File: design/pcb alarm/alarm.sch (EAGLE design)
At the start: 5 parts, among them IC1 7805T

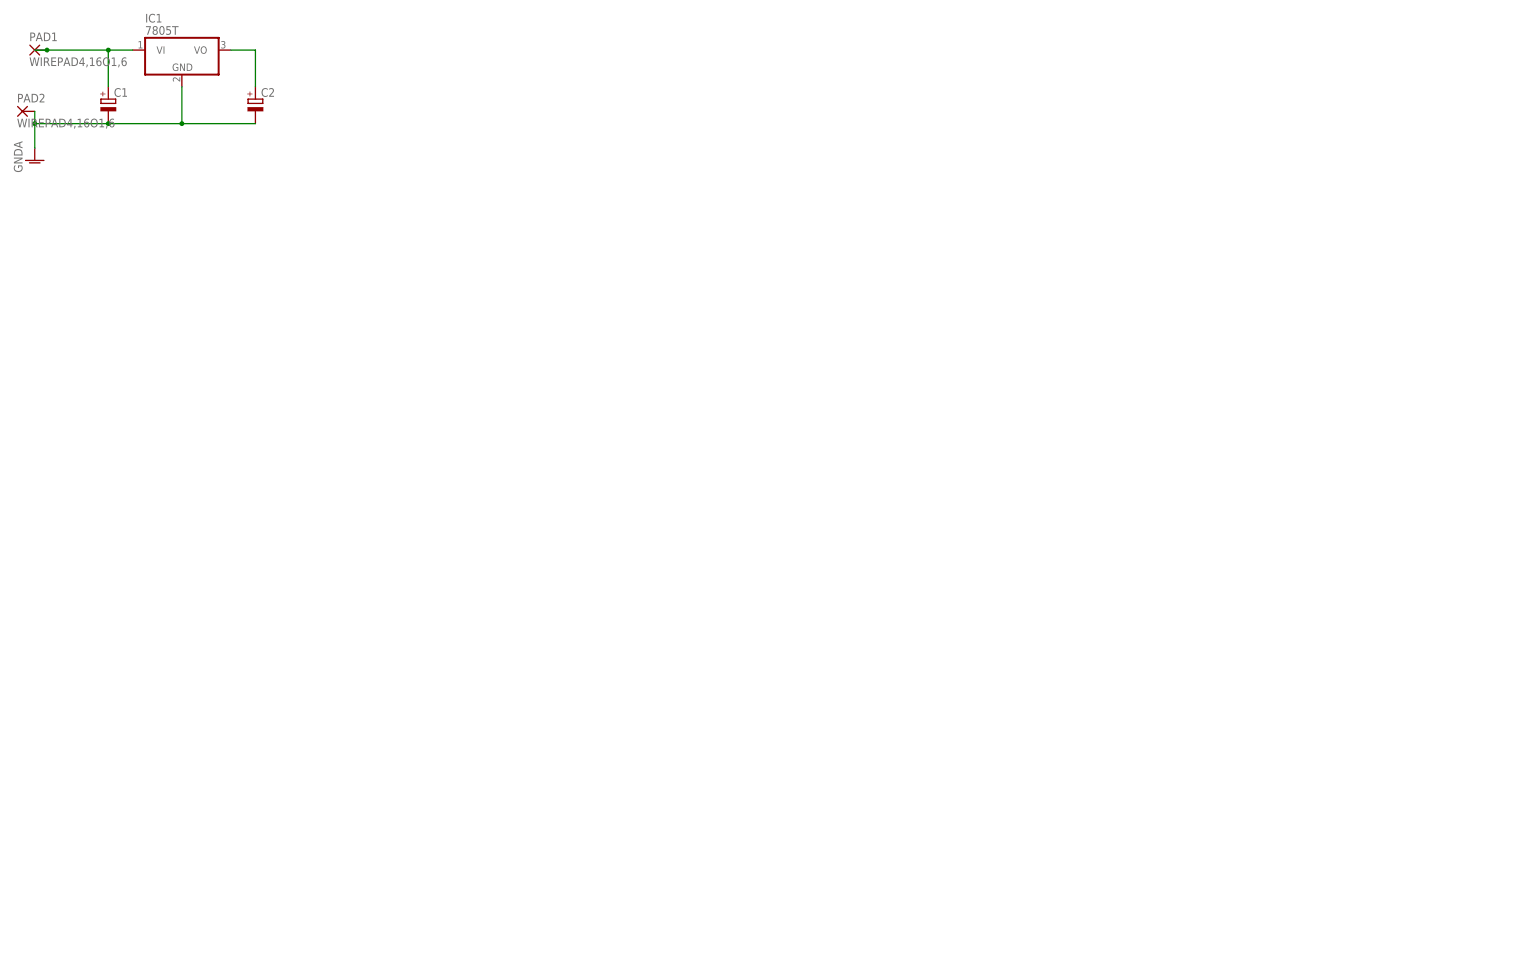
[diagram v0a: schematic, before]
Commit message: 8
pembuatan desain alarm esw untuk ews banjir
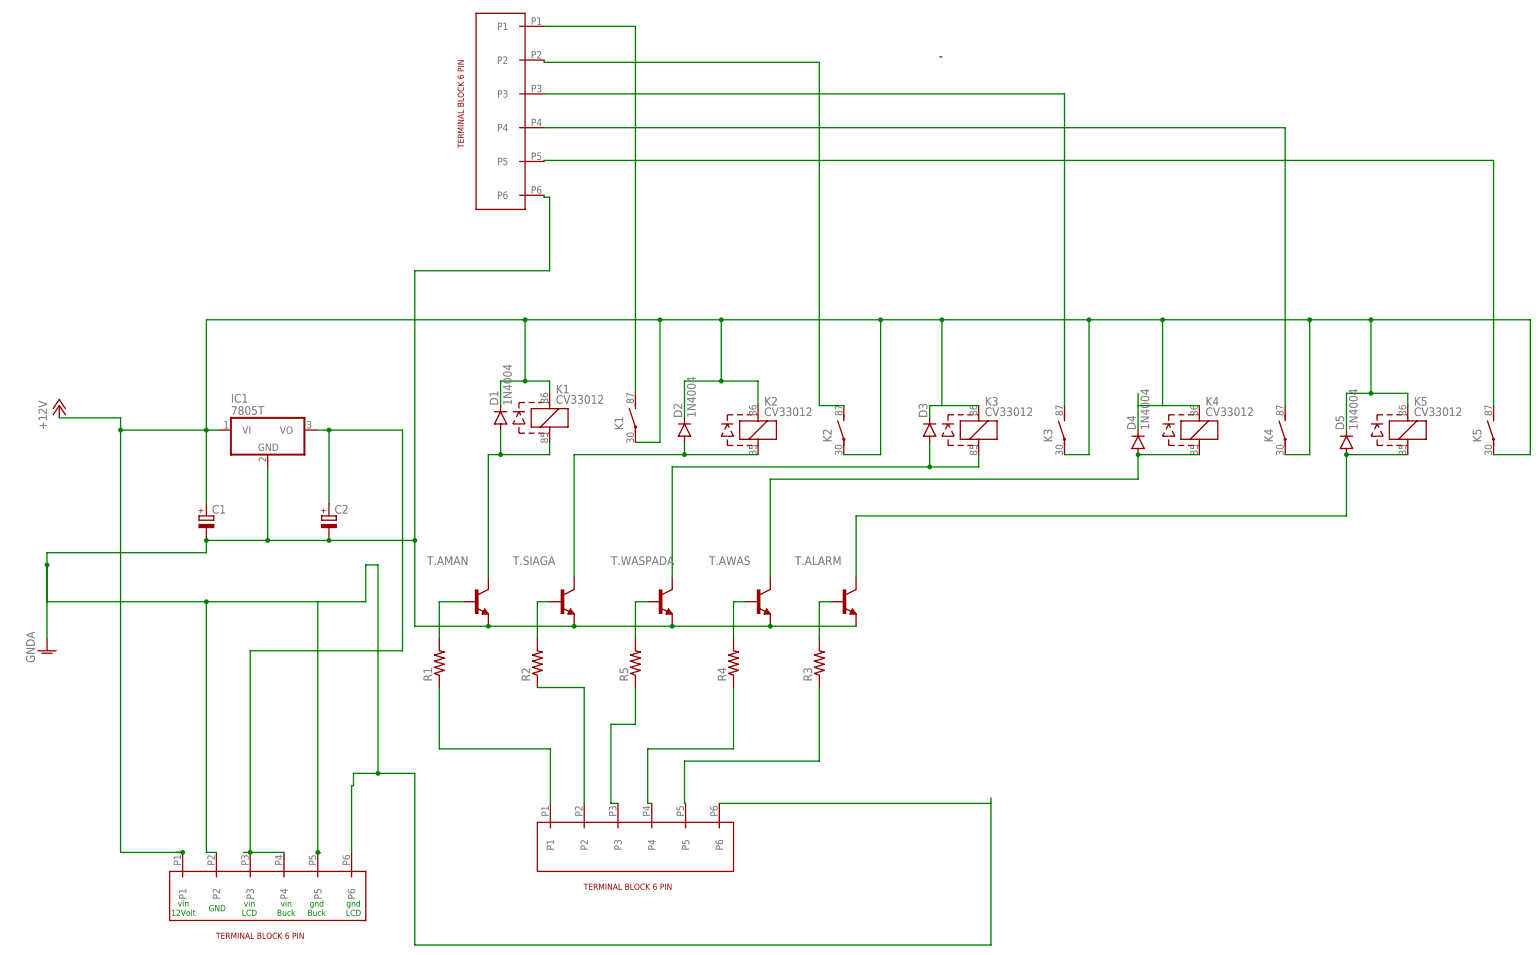
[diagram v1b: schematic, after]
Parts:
- removed PAD1, PAD2: WIREPAD4,16O1,6, wirepad:WIREPAD4,16O1,6
- added D1, D2, D3, D4, D5: 1N4004, diode:1N4004
- added K1, K2, K3, K4, K5: CV33012, relay:CV33012
- added R1, R2, R3, R4, R5: (no value), rcl:R-US_0204/5
- added T.ALARM, T.AMAN, T.AWAS, T.SIAGA, T.WASPADA: (no value), transistor-neu-to92:2N2222-NPN-TO92-EBC
- added U$1, U$6, U$7: TERMINAL-BLOCK-6-PIN, TERMINAL-BLOCK-6-PIN:TERMINAL-BLOCK-6-PIN
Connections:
- new net +12V: C1.+, D1.C, D2.C, D3.C, D4.C, D5.C, IC1.VI, K1G$1.+, K1G$2.P, K2G$1.+, K2G$2.P, K3G$1.+, K3G$2.P, K4G$1.+, K4G$2.P, K5G$1.+, K5G$2.P, U$7.P1
- new net N$10: K3G$2.S, U$1.P3
- new net N$11: K4G$2.S, U$1.P4
- new net N$12: K5G$2.S, U$1.P5
- new net N$13: R2.1, U$6.P2
- new net N$14: R5.1, U$6.P3
- new net N$15: R4.1, U$6.P4
- new net N$16: R3.1, U$6.P5
- new net N$17: C2.+, IC1.VO, U$7.P3, U$7.P4
- new net N$27: D1.A, K1G$1.-, T.AMAN.C
- new net N$29: D4.A, K4G$1.-, T.AWAS.C
- new net N$3: R1.1, U$6.P1
- new net N$31: D3.A, K3G$1.-, T.WASPADA.C
- new net N$32: D2.A, K2G$1.-, T.SIAGA.C
- new net N$4: R2.2, T.SIAGA.B
- new net N$5: R5.2, T.WASPADA.B
- new net N$6: R4.2, T.AWAS.B
- new net N$7: R3.2, T.ALARM.B
- new net N$8: K2G$2.S, U$1.P2
- new net N$9: D5.A, K5G$1.-, T.ALARM.C
- net GNDA: now also T.ALARM.E, T.AMAN.E, T.AWAS.E, T.SIAGA.E, T.WASPADA.E, U$1.P6, U$6.P6, U$7.P2, U$7.P5, U$7.P6; no longer PAD2.P
- net N$1: now also K1G$2.S, U$1.P1; no longer C1.+, IC1.VI, PAD1.P
- net N$2: now also R1.2, T.AMAN.B; no longer C2.+, IC1.VO
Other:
- note added: "GND"
- note added: "gnd Buck"
- note added: "gnd LCD"
- note added: "vin 12Volt"
- note added: "vin Buck"
- note added: "vin LCD"
- moved on the sheet: C1, C2, IC1
